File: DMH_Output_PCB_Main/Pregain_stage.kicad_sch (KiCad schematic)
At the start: 11 parts, among them J29 Conn_01x04_PinHeader, J30 Conn_01x04_PinHeader, U7 TL072

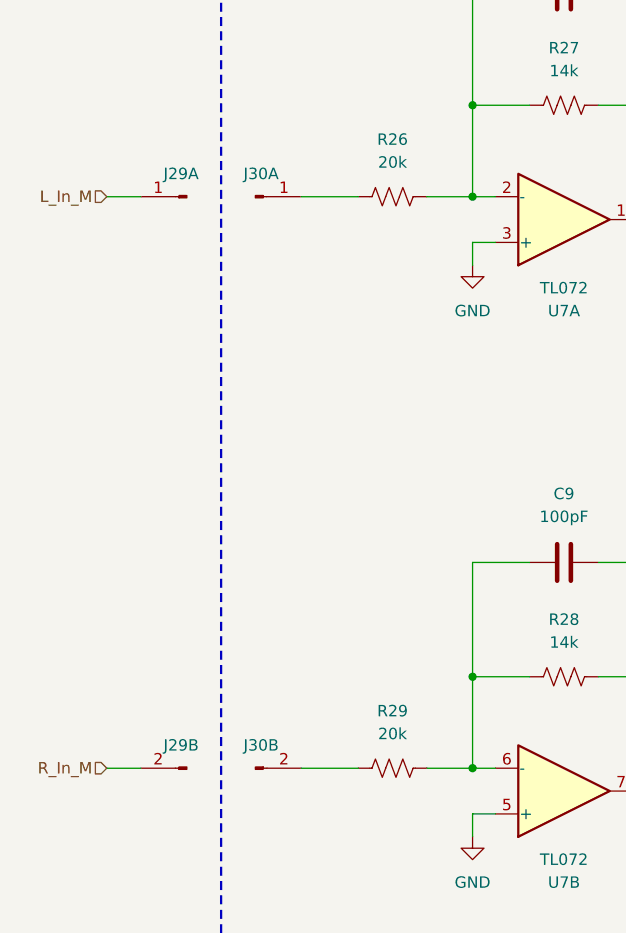
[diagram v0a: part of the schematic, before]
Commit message: Placed pin sockets
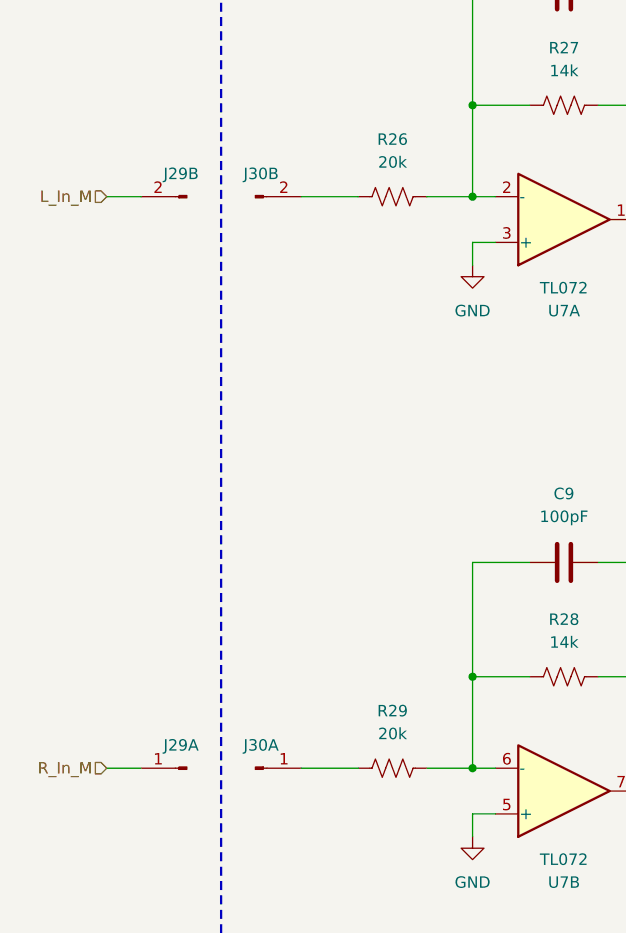
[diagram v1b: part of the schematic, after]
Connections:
- net L_In_M: now also J29.2 (Pin_2); no longer J29.1 (Pin_1)
- net R_In_M: now also J29.1 (Pin_1); no longer J29.2 (Pin_2)
- net at J30.2 (Pin_2): now also R26.1; no longer R29.1
- net at J30.1 (Pin_1): now also R29.1; no longer R26.1
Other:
- moved on the sheet: J29A, J29B, J30A, J30B
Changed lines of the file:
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@@
 	(symbol
 		(lib_id "SynthStuff:Conn_01x04_PinHeader")
-		(at 54.61 124.46 0)
+		(at 54.61 60.96 0)
 		(unit 2)
 		(body_style 1)
@@
 		(fields_autoplaced yes)
 		(property "Reference" "J30"
-			(at 55.245 121.92 0)
+			(at 55.245 58.42 0)
 			(show_name no)
 			(do_not_autoplace no)
@@
 		)
 		(property "Value" "Conn_01x04_PinHeader"
-			(at 54.61 127 0)
+			(at 54.61 63.5 0)
 			(hide yes)
 			(show_name no)
@@
 		)
 		(property "Footprint" "Connector_PinHeader_2.54mm:PinHeader_1x04_P2.54mm_Vertical"
-			(at 54.61 124.46 0)
-			(hide yes)
-			(show_name no)
-			(do_not_autoplace no)
-			(effects
-				(font
-					(size 1.27 1.27)
-				)
-			)
-		)
-		(property "Datasheet" ""
-			(at 54.61 124.46 0)
+			(at 54.61 60.96 0)
+			(hide yes)
+			(show_name no)
+			(do_not_autoplace no)
+			(effects
+				(font
+					(size 1.27 1.27)
+				)
+			)
+		)
+		(property "Datasheet" ""
+			(at 54.61 60.96 0)
 			(hide yes)
 			(show_name no)
@@
 		)
 		(property "Description" "Generic connector, single row, 01x04"
-			(at 54.61 124.46 0)
+			(at 54.61 60.96 0)
 			(hide yes)
 			(show_name no)
@@
 	(symbol
 		(lib_id "SynthStuff:Conn_01x04_PinHeader")
-		(at 54.61 60.96 0)
+		(at 54.61 124.46 0)
 		(unit 1)
 		(body_style 1)
@@
 		(fields_autoplaced yes)
 		(property "Reference" "J30"
-			(at 55.245 58.42 0)
+			(at 55.245 121.92 0)
 			(show_name no)
 			(do_not_autoplace no)
@@
 		)
 		(property "Value" "Conn_01x04_PinHeader"
-			(at 54.61 63.5 0)
+			(at 54.61 127 0)
 			(hide yes)
 			(show_name no)
@@
 		)
 		(property "Footprint" "Connector_PinHeader_2.54mm:PinHeader_1x04_P2.54mm_Vertical"
-			(at 54.61 60.96 0)
-			(hide yes)
-			(show_name no)
-			(do_not_autoplace no)
-			(effects
-				(font
-					(size 1.27 1.27)
-				)
-			)
-		)
-		(property "Datasheet" ""
-			(at 54.61 60.96 0)
+			(at 54.61 124.46 0)
+			(hide yes)
+			(show_name no)
+			(do_not_autoplace no)
+			(effects
+				(font
+					(size 1.27 1.27)
+				)
+			)
+		)
+		(property "Datasheet" ""
+			(at 54.61 124.46 0)
 			(hide yes)
 			(show_name no)
@@
 		)
 		(property "Description" "Generic connector, single row, 01x04"
-			(at 54.61 60.96 0)
+			(at 54.61 124.46 0)
 			(hide yes)
 			(show_name no)
@@
 	(symbol
 		(lib_id "SynthStuff:Conn_01x04_PinHeader")
+		(at 46.99 124.46 180)
+		(unit 1)
+		(body_style 1)
+		(exclude_from_sim no)
+		(in_bom yes)
+		(on_board yes)
+		(in_pos_files yes)
+		(dnp no)
+		(fields_autoplaced yes)
+		(property "Reference" "J29"
+			(at 46.355 121.92 0)
+			(show_name no)
+			(do_not_autoplace no)
+			(effects
+				(font
+					(size 1.27 1.27)
+				)
+			)
+		)
+		(property "Value" "Conn_01x04_PinHeader"
+			(at 46.99 121.92 0)
+			(hide yes)
+			(show_name no)
+			(do_not_autoplace no)
+			(effects
+				(font
+					(size 1.27 1.27)
+				)
+			)
+		)
+		(property "Footprint" "Connector_PinSocket_2.54mm:PinSocket_1x04_P2.54mm_Vertical"
+			(at 46.99 124.46 0)
+			(hide yes)
+			(show_name no)
+			(do_not_autoplace no)
+			(effects
+				(font
+					(size 1.27 1.27)
+				)
+			)
+		)
+		(property "Datasheet" ""
+			(at 46.99 124.46 0)
+			(hide yes)
+			(show_name no)
+			(do_not_autoplace no)
+			(effects
+				(font
+					(size 1.27 1.27)
+				)
+			)
+		)
+		(property "Description" "Generic connector, single row, 01x04"
+			(at 46.99 124.46 0)
+			(hide yes)
+			(show_name no)
+			(do_not_autoplace no)
+			(effects
+				(font
+					(size 1.27 1.27)
+				)
+			)
+		)
+		(pin "4"
+		)
+		(pin "2"
+		)
+		(pin "1"
+		)
+		(pin "3"
+		)
+		(instances
+			(project "DMH_Output_PCB_Main"
+				(path "/58f4306d-5387-4983-bb08-41a2313fd315/0b1658b3-ac7b-4692-8043-3e4b42d6c671"
+					(reference "J29")
+					(unit 1)
+				)
+			)
+		)
+	)
+	(symbol
+		(lib_id "SynthStuff:Conn_01x04_PinHeader")
 		(at 46.99 60.96 180)
-		(unit 1)
+		(unit 2)
 		(body_style 1)
 		(exclude_from_sim no)
@@
 			(hide yes)
 			(show_name no)
-			(do_not_autoplace no)
-			(effects
-				(font
-					(size 1.27 1.27)
-				)
-			)
-		)
-		(pin "4"
-		)
-		(pin "2"
-		)
-		(pin "1"
-		)
-		(pin "3"
-		)
-		(instances
-			(project "DMH_Output_PCB_Main"
-				(path "/58f4306d-5387-4983-bb08-41a2313fd315/0b1658b3-ac7b-4692-8043-3e4b42d6c671"
-					(reference "J29")
-					(unit 1)
-				)
-			)
-		)
-	)
-	(symbol
-		(lib_id "SynthStuff:Conn_01x04_PinHeader")
-		(at 46.99 124.46 180)
-		(unit 2)
-		(body_style 1)
-		(exclude_from_sim no)
-		(in_bom yes)
-		(on_board yes)
-		(in_pos_files yes)
-		(dnp no)
-		(fields_autoplaced yes)
-		(property "Reference" "J29"
-			(at 46.355 121.92 0)
-			(show_name no)
-			(do_not_autoplace no)
-			(effects
-				(font
-					(size 1.27 1.27)
-				)
-			)
-		)
-		(property "Value" "Conn_01x04_PinHeader"
-			(at 46.99 121.92 0)
-			(hide yes)
-			(show_name no)
-			(do_not_autoplace no)
-			(effects
-				(font
-					(size 1.27 1.27)
-				)
-			)
-		)
-		(property "Footprint" "Connector_PinSocket_2.54mm:PinSocket_1x04_P2.54mm_Vertical"
-			(at 46.99 124.46 0)
-			(hide yes)
-			(show_name no)
-			(do_not_autoplace no)
-			(effects
-				(font
-					(size 1.27 1.27)
-				)
-			)
-		)
-		(property "Datasheet" ""
-			(at 46.99 124.46 0)
-			(hide yes)
-			(show_name no)
-			(do_not_autoplace no)
-			(effects
-				(font
-					(size 1.27 1.27)
-				)
-			)
-		)
-		(property "Description" "Generic connector, single row, 01x04"
-			(at 46.99 124.46 0)
-			(hide yes)
-			(show_name no)
